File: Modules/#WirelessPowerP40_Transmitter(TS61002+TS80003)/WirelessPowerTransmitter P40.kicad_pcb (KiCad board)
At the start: 4 copper layers, 53 x 49 mm, 119 parts, among them J1 USBA, J2 I2C, J3 I2C, J4 Coil Therm, J5 COIL 20uH, U1 TS30041, U2 TS94033, U3 74LVC1G66, U4 TS61002, U5 TS80003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

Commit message: WirelessPowerP40_Transmitter update
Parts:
- J2, J3: footprint Connector_PinHeader_2.00mm:PinHeader_1x02_P2.00mm_Vertical -> Connector_PinHeader_2.00mm:PinHeader_1x04_P2.00mm_Vertical
- moved J3 8.32 mm to (134.4, 71.2)
- moved C4 2.03 mm to (129.5, 82.1), turned to 0 degrees
- moved C19 1.99 mm to (124.0, 93.4)
- moved C6 1.99 mm to (124.0, 85.2)
- moved C8 1.99 mm to (124.0, 89.2)
- moved D3 1.99 mm to (126.0, 93.4)
- moved C15 1.99 mm to (131.5, 83.8)
- moved C17 1.99 mm to (133.4, 85.6)
- moved C3 1.99 mm to (131.5, 89.6)
- moved C5 1.99 mm to (126.0, 85.2)
- moved C9 1.99 mm to (126.0, 89.2)
- moved R12 1.99 mm to (129.0, 91.3)
- moved R2 1.99 mm to (131.5, 93.8)
- moved R8 1.99 mm to (131.5, 85.7)
- moved C13 1.99 mm to (131.5, 87.6)
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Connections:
- J2 pad 1: Net-(J2-Pad1) -> +3V3
- J3 pad 1: Net-(J3-Pad1) -> +3V3
- R21 pad 2: Net-(J3-Pad1) -> Net-(J3-Pad3)
- R39 pad 2: Net-(J2-Pad1) -> Net-(J2-Pad3)
- U5 pad 19: Net-(J2-Pad1) -> Net-(J2-Pad3)
- U5 pad 40: Net-(J3-Pad1) -> Net-(J3-Pad3)
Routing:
- net COIL-: track 118.9 -> 29.1 mm
- net Net-(C37-Pad2): track 140.9 -> 70.3 mm
- net Net-(C36-Pad2): track 121.6 -> 55.4 mm
- net +3V3: track 59.5 -> 86.7 mm, vias 6 -> 5
- net Net-(J3-Pad3): track 0.00 -> 17.1 mm, vias 0 -> 1
- net Net-(J3-Pad1): track 15.4 -> 0.00 mm, vias 1 -> 0
- net Net-(J2-Pad3): track 0.00 -> 12.8 mm, vias 0 -> 1
- net Net-(J2-Pad1): track 11.9 -> 0.00 mm, vias 1 -> 0
- net SYNC1: track 32.2 -> 24.3 mm
- net DC_I-: track 32.7 -> 25.8 mm
- net SYNC2: track 29.1 -> 23.6 mm
- net VDDA: track 57.6 -> 53.4 mm, vias 4 -> 6
- net Net-(J3-Pad2): track 13.9 -> 16.6 mm
- net PWM1_L: track 39.5 -> 37.0 mm
- net DRV_EN: track 49.4 -> 47.0 mm
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- added copper zone on F.Cu, net COIL-
- added copper zone on F.Cu, net Net-(C36-Pad2)
- added copper zone on F.Cu, net Net-(C37-Pad2)
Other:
- board text added: "+"
- board text added: "-"
- board text added: "R"
- board text added: "T"

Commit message: WirelessPowerP40_Transmitter update
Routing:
- net +5V: track 49.6 -> 44.7 mm
- net DC_I+: track 143.7 -> 139.8 mm
- net GND: vias 290 -> 285

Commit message: WirelessPowerP40_Transmitter update
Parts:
- moved C9 2.02 mm to (124.0, 89.5)
- moved C8 2.02 mm to (126.0, 89.5)
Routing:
- net DC_I+: track 139.8 -> 106.3 mm
- net GND: track 48.7 -> 35.5 mm
- added copper zone on F.Cu, net DC_I+

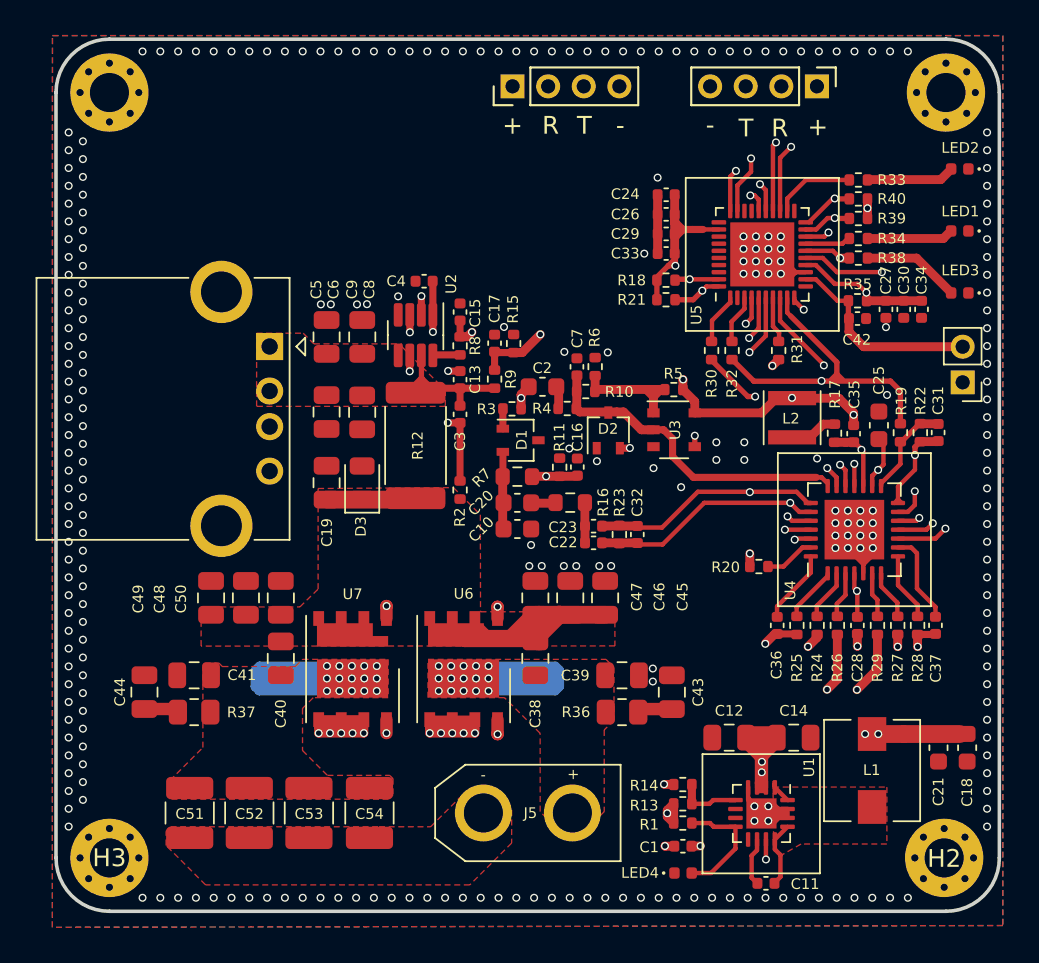
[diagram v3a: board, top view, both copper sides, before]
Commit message: add simple cooler controller for WirelessPowerTransmitter P40
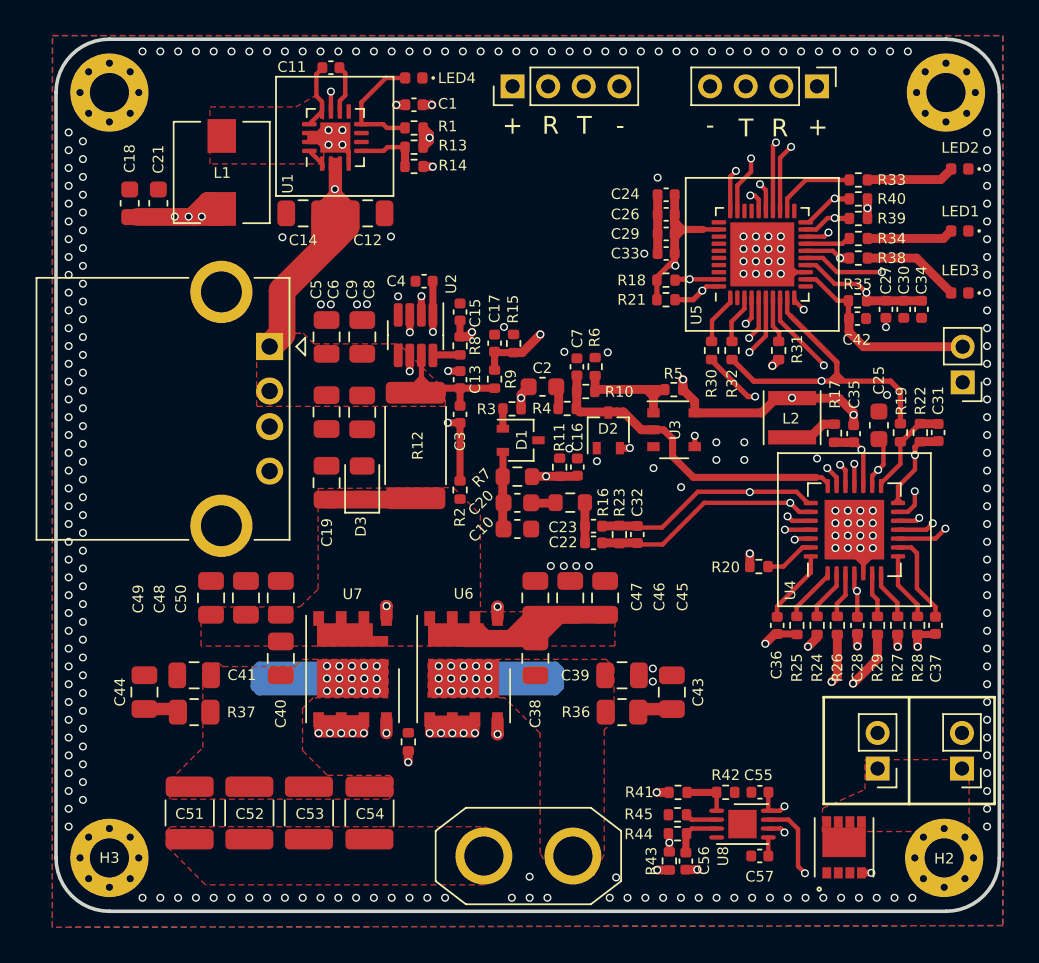
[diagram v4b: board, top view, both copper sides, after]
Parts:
- added C55: 4.7uF, Capacitor_SMD:C_0402_1005Metric, F.Cu at (148.3, 110.8)
- added C56: 1uF, Capacitor_SMD:C_0402_1005Metric, F.Cu at (144.2, 114.7)
- added C57: 330nF, Capacitor_SMD:C_0402_1005Metric, F.Cu at (148.3, 114.4)
- added J6: Conn_01x02_Male, Connector_PinHeader_2.00mm:PinHeader_1x02_P2.00mm_Vertical, F.Cu at (159.7, 109.5)
- added J7: Conn_01x02_Male, Connector_PinHeader_2.00mm:PinHeader_1x02_P2.00mm_Vertical, F.Cu at (155.0, 109.5)
- added NCP15XW153J03RC1: Thermistor_NTC, Resistor_SMD:R_0402_1005Metric, F.Cu at (128.6, 108.0)
- added R41: 32K, Resistor_SMD:R_0402_1005Metric, F.Cu at (143.7, 110.8)
- added R42: 200K, Resistor_SMD:R_0402_1005Metric, F.Cu at (146.4, 110.8)
- added R43: 12.4K, Resistor_SMD:R_0402_1005Metric, F.Cu at (143.3, 114.7)
- added R44: 5M, Resistor_SMD:R_0402_1005Metric, F.Cu at (143.7, 113.1)
- added R45: 12.4K, Resistor_SMD:R_0402_1005Metric, F.Cu at (143.7, 112.1)
- added U8: max31740, Package_DFN_QFN:TDFN-8-1EP_3x2mm_P0.5mm_EP1.80x1.65mm, F.Cu at (147.4, 112.6)
- added U9: CSD16406Q3, lib:CSD16406Q3, F.Cu at (153.1, 113.9)
- C51, C52, C53, C54: footprint Inductor_SMD:L_1210_3225Metric -> Capacitor_SMD:C_1210_3225Metric
- moved C18 56.1 mm to (112.9, 77.7), turned to 90 degrees
- moved C21 53.4 mm to (114.5, 77.7), turned to 90 degrees
- moved C11 51.9 mm to (124.2, 70.1), turned to 180 degrees
- moved L1 49.6 mm to (118.1, 76.0), turned to -90 degrees
- moved LED4 47.2 mm to (128.9, 70.7), turned to 180 degrees
- moved U1 44.9 mm to (124.5, 74.0), turned to 90 degrees
- moved C1 44.3 mm to (128.9, 72.2), turned to 0 degrees
- moved R1 41.9 mm to (128.9, 73.5), turned to 0 degrees
- moved C14 40.3 mm to (122.7, 78.3), turned to 180 degrees
- moved R13 39.9 mm to (128.9, 74.6), turned to 0 degrees
- moved R14 37.9 mm to (128.9, 75.7), turned to 180 degrees
- moved C12 35.8 mm to (126.3, 78.3), turned to 0 degrees
- moved J5 2.42 mm to (132.8, 114.4)
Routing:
- net +5V: track 44.7 -> 123.6 mm, vias 5 -> 11
- net DC_I+: track 106.3 -> 55.7 mm, vias 4 -> 3
- net Net-(NCP15XW153J03RC1-Pad1): track 0.00 -> 18.2 mm, vias 0 -> 2
- net Net-(U8-Pad7): track 0.00 -> 8.82 mm, vias 0 -> 2
- net Net-(C56-Pad2): track 0.00 -> 2.89 mm
- net Net-(R41-Pad1): track 0.00 -> 2.70 mm
- net Net-(R45-Pad1): track 0.00 -> 1.80 mm
- net Net-(C57-Pad1): track 0.00 -> 0.96 mm
- net COIL-: track 29.1 -> 28.1 mm
- net Net-(R29-Pad2): track 32.9 -> 32.2 mm
- net GND: vias 285 -> 281
- added copper zone on In2.Cu, net +5V
- added copper zone on F.Cu, net Net-(J6-Pad1)

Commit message: WirelessPowerP40_Transmitter update
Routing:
- net GND: track 35.5 -> 35.4 mm, vias 281 -> 295

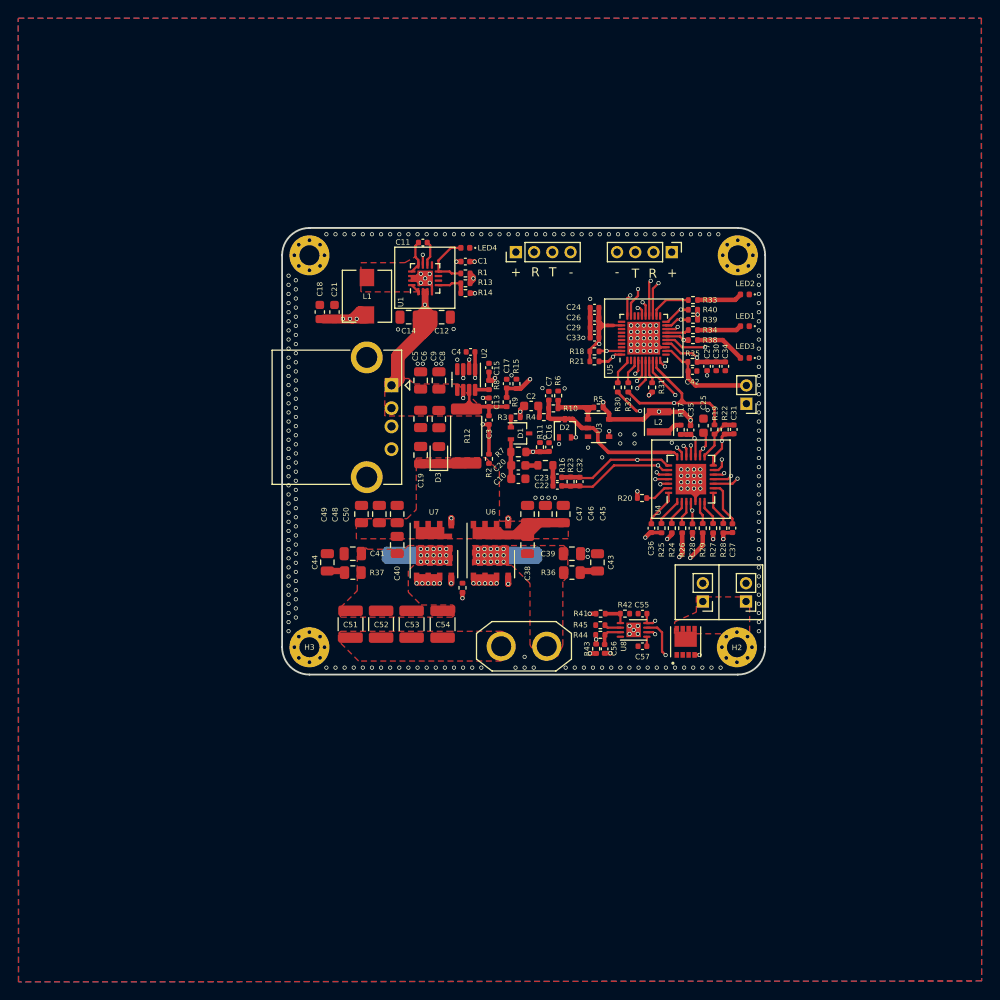
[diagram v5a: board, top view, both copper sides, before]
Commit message: change WirelessPowerTransmitter P40 usb connector
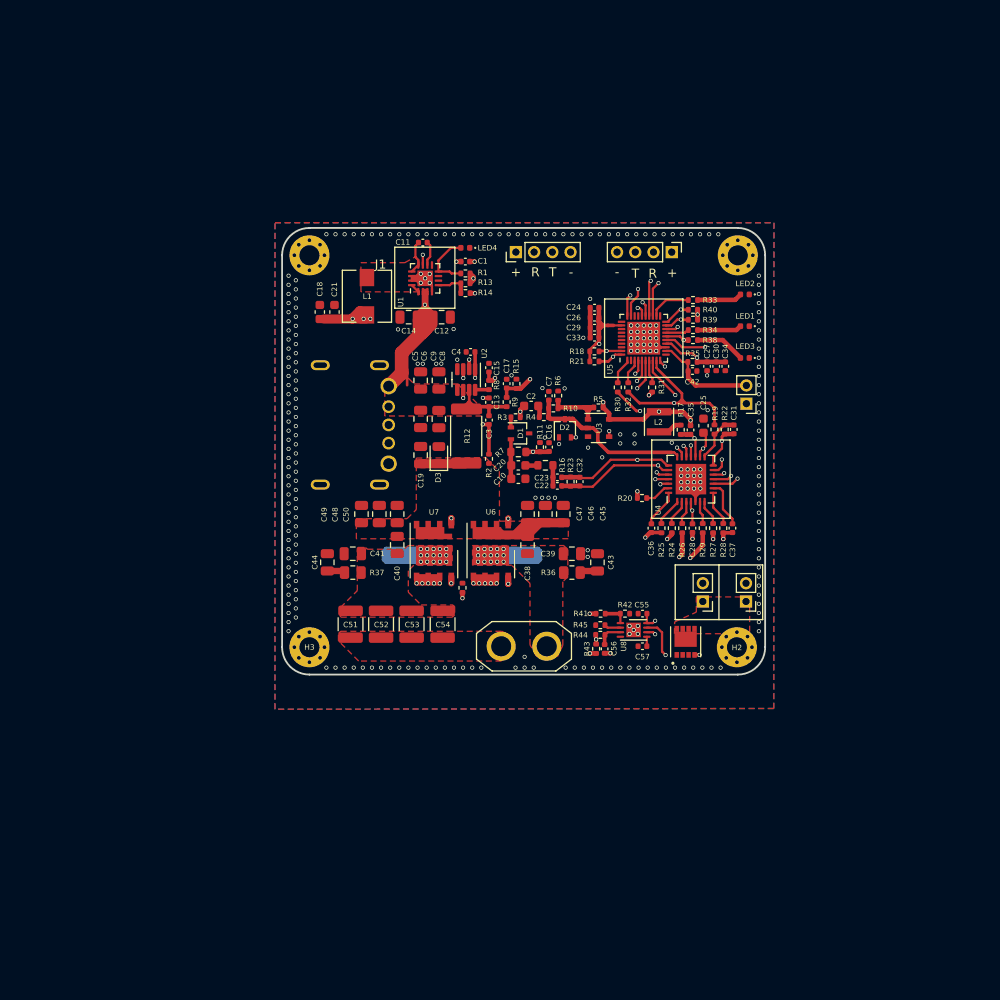
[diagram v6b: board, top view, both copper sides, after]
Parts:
- J1: footprint Connector_USB:USB_A_CONNFLY_DS1095-WNR0 -> USB_plug:USB_A_2.0_FAST
- moved J1 4.53 mm to (119.5, 90.1), turned to 0 degrees
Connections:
- J1 pad 5: GND -> unconnected-(J1-Pad5)
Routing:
- net +5V: track 123.6 -> 118.3 mm
- net DC_I+: track 55.7 -> 57.3 mm

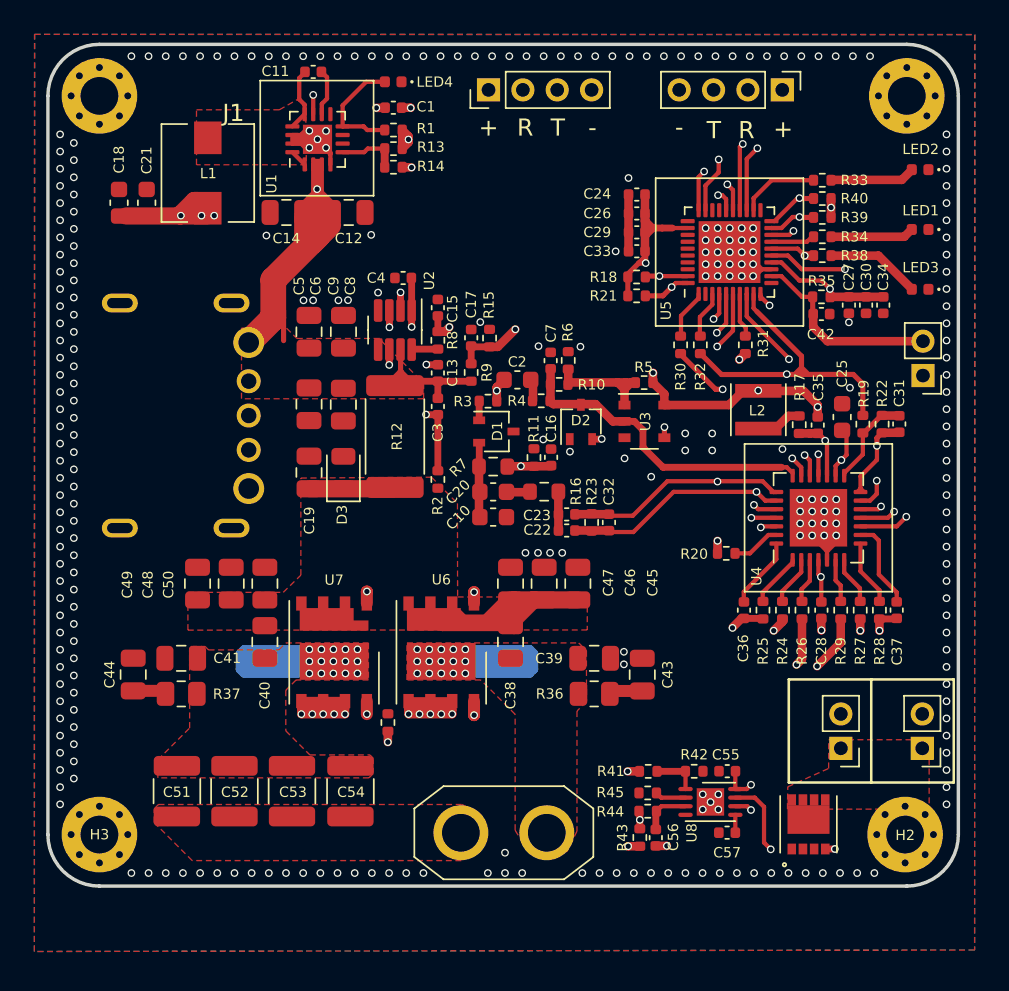
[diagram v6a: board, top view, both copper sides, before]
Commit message: Outshape optimization of WirelessPowerTransmitterP40
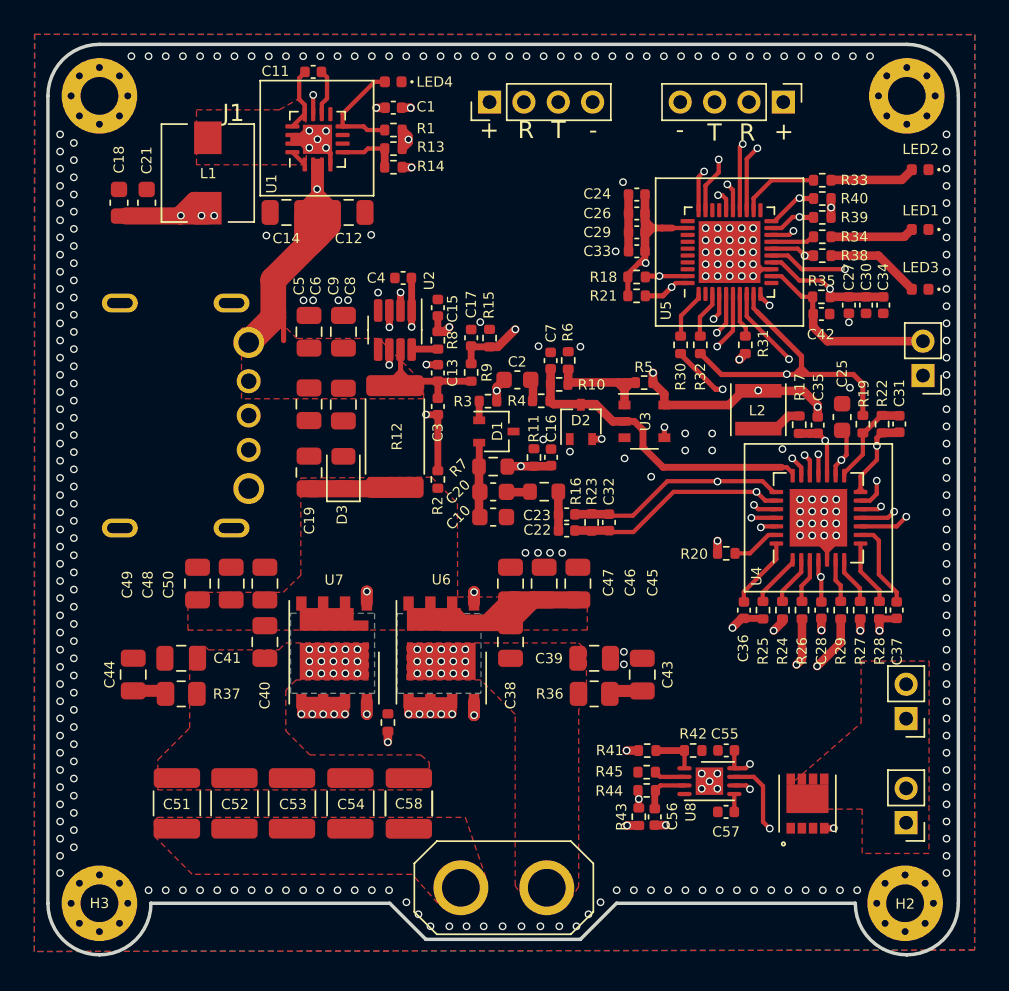
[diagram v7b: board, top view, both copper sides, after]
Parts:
- added C58: NP, Capacitor_SMD:C_1210_3225Metric, F.Cu at (129.8, 112.7)
- moved J7 5.76 mm to (158.8, 113.8)
- moved H2 4.00 mm to (158.7, 118.5)
- moved H3 4.00 mm to (111.8, 118.5)
- moved J5 3.20 mm to (132.8, 117.6)
- moved J6 1.97 mm to (158.8, 107.8)
- moved C55 1.21 mm to (148.3, 109.6)
- moved C56 1.21 mm to (144.1, 113.5)
- moved U8 1.21 mm to (147.3, 111.4)
- moved C57 1.21 mm to (148.3, 113.2)
- moved R41 1.21 mm to (143.7, 109.6)
- moved R42 1.21 mm to (146.4, 109.6)
- moved R43 1.21 mm to (143.2, 113.5)
- moved R44 1.21 mm to (143.7, 111.9)
- moved R45 1.21 mm to (143.7, 110.9)
- moved U9 1.21 mm to (153.0, 112.7)
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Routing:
- net Net-(C36-Pad2): track 55.4 -> 18.0 mm
- net Net-(C37-Pad2): track 70.0 -> 34.0 mm
- net COIL-: track 28.1 -> 31.2 mm
- net +3V3: track 86.7 -> 85.0 mm
- net Net-(J3-Pad2): track 16.6 -> 15.8 mm
- net Net-(J2-Pad3): track 12.8 -> 12.0 mm
- net Net-(J2-Pad2): track 10.4 -> 9.65 mm
- net Net-(J3-Pad3): track 17.1 -> 16.4 mm
- net Net-(NCP15XW153J03RC1-Pad1): track 18.2 -> 17.6 mm
- net GND: vias 295 -> 310
- added copper zone on B.Cu, net Net-(C36-Pad2)
- added copper zone on B.Cu, net Net-(C37-Pad2)
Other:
- board size 53 x 49 mm -> 53 x 53 mm

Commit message: Wrong Silk text fix
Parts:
- moved R12 0.09 mm to (129.0, 91.4)
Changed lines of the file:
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@@
   (net 92 "unconnected-(J1-Pad5)")
   (footprint "Resistor_SMD:R_2512_6332Metric" (layer "F.Cu")
-    (at 129 91.33 -90)
+    (at 128.99 91.42 -90)
     (descr "Resistor SMD 2512 (6332 Metric), square (rectangular) end terminal, IPC_7351 nominal, (Body size source: IPC-SM-782 page 72, https://www.pcb-3d.com/wordpress/wp-content/uploads/ipc-sm-782a_amendment_1_and_2.pdf), generated with kicad-footprint-generator")
     (tags "resistor")
@@
     (property "Sheetname" "")
     (attr smd)
-    (fp_text reference "J1" (at 0.11 -17.61 unlocked) (layer "F.SilkS")
+    (fp_text reference "J1" (at -1.37 0.2425 unlocked) (layer "F.SilkS") hide
       (effects (font (size 1 1) (thickness 0.15)))
     )
@@
   (gr_line (start 141.9 118.5) (end 139.8 120.6) (layer "Edge.Cuts") (width 0.2))
   (gr_arc (start 161.8 118.5) (mid 160.92132 120.62132) (end 158.8 121.5) (layer "Edge.Cuts") (width 0.2))
-  (gr_text "+" (at 134.49 73.49) (layer "F.SilkS")
+  (gr_text "+" (at 151.724285 73.77 180) (layer "F.SilkS")
     (effects (font (size 1 1) (thickness 0.15)))
   )
-  (gr_text "R" (at 136.625714 73.49) (layer "F.SilkS")
+  (gr_text "R" (at 149.588573 73.77 180) (layer "F.SilkS")
     (effects (font (size 1 1) (thickness 0.15)))
   )
-  (gr_text "T" (at 147.606669 73.64) (layer "F.SilkS")
+  (gr_text "T" (at 138.607617 73.62 180) (layer "F.SilkS")
     (effects (font (size 1 1) (thickness 0.15)))
   )
-  (gr_text "-" (at 145.59 73.64 180) (layer "F.SilkS")
+  (gr_text "-" (at 140.624286 73.62) (layer "F.SilkS")
     (effects (font (size 1 1) (thickness 0.15)))
   )
-  (gr_text "+" (at 151.64 73.64 180) (layer "F.SilkS")
+  (gr_text "+" (at 134.574286 73.62) (layer "F.SilkS")
     (effects (font (size 1 1) (thickness 0.15)))
   )
-  (gr_text "T" (at 138.523332 73.49) (layer "F.SilkS")
+  (gr_text "T" (at 147.690954 73.77 180) (layer "F.SilkS")
     (effects (font (size 1 1) (thickness 0.15)))
   )
-  (gr_text "-" (at 140.54 73.49) (layer "F.SilkS")
+  (gr_text "-" (at 145.674285 73.77 180) (layer "F.SilkS")
     (effects (font (size 1 1) (thickness 0.15)))
   )
-  (gr_text "R" (at 149.504286 73.64) (layer "F.SilkS")
+  (gr_text "R" (at 136.71 73.62 180) (layer "F.SilkS")
     (effects (font (size 1 1) (thickness 0.15)))
   )
